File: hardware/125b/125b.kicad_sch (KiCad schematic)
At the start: 49 parts, among them J1 Guitar in, J2 Barrel_Jack, J3 Conn_02x05_Odd_Even_MountingP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, J4 Guitar out, SW1 SW_DIP_x02, SW2 RotaryEncoder_Switch, SW3 Switch 1, SW4 Switch 2, U1 L78L05_TO92, U2 TL074

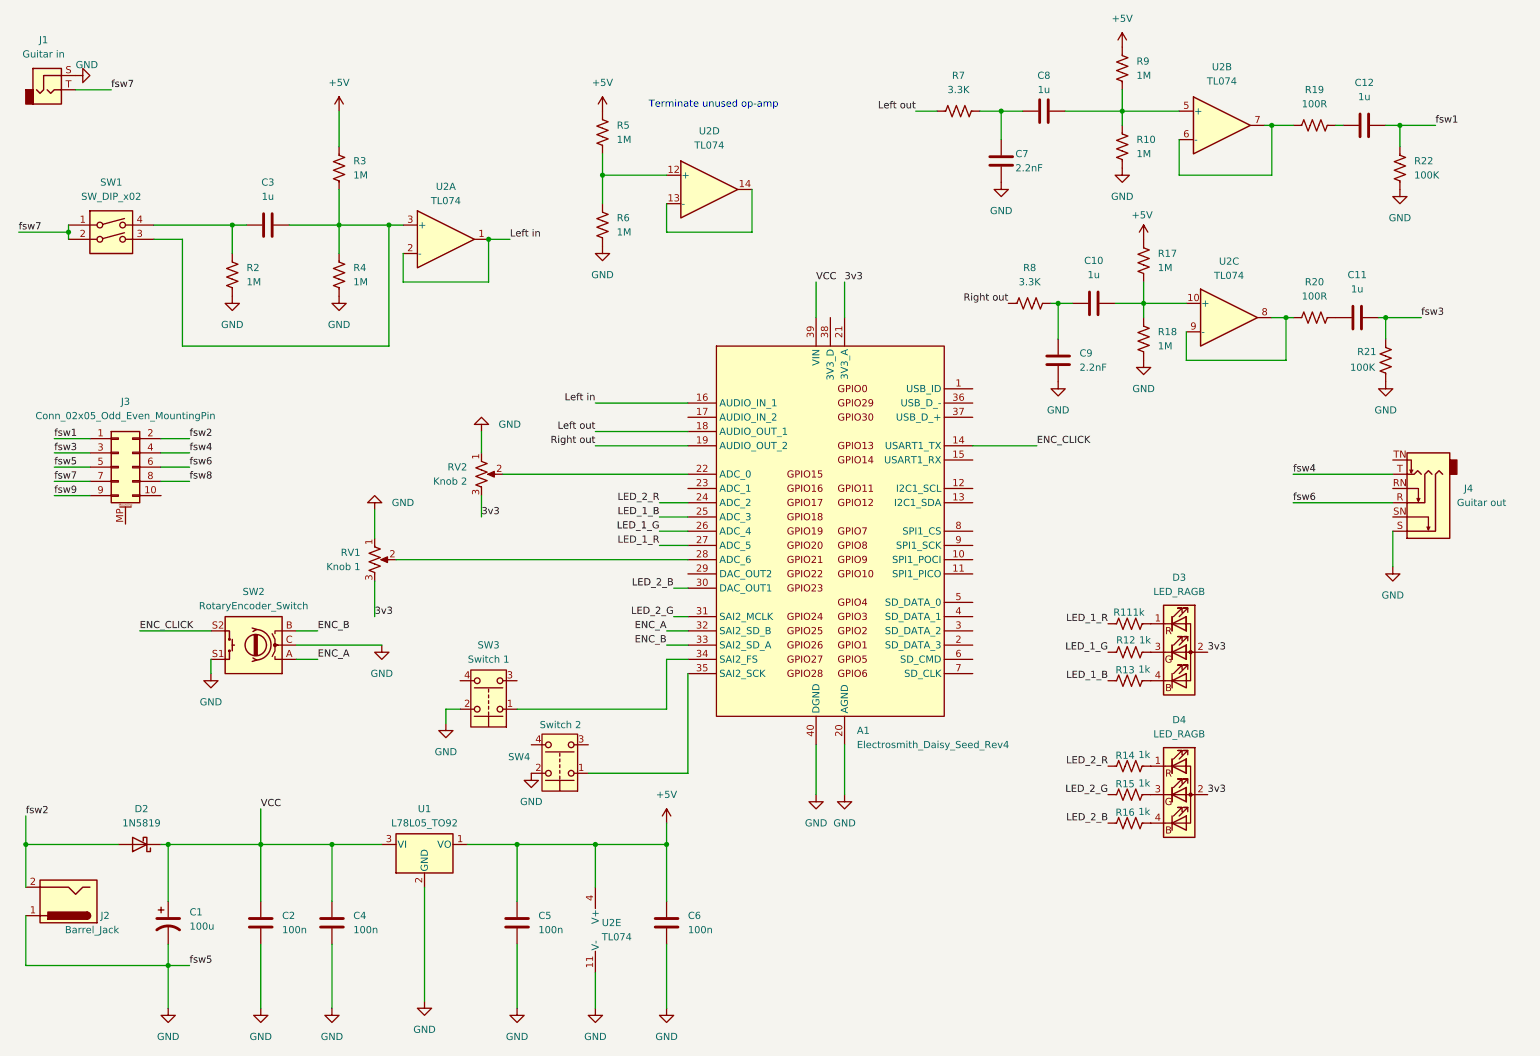
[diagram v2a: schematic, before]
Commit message: All components connected with new IDC socket pos
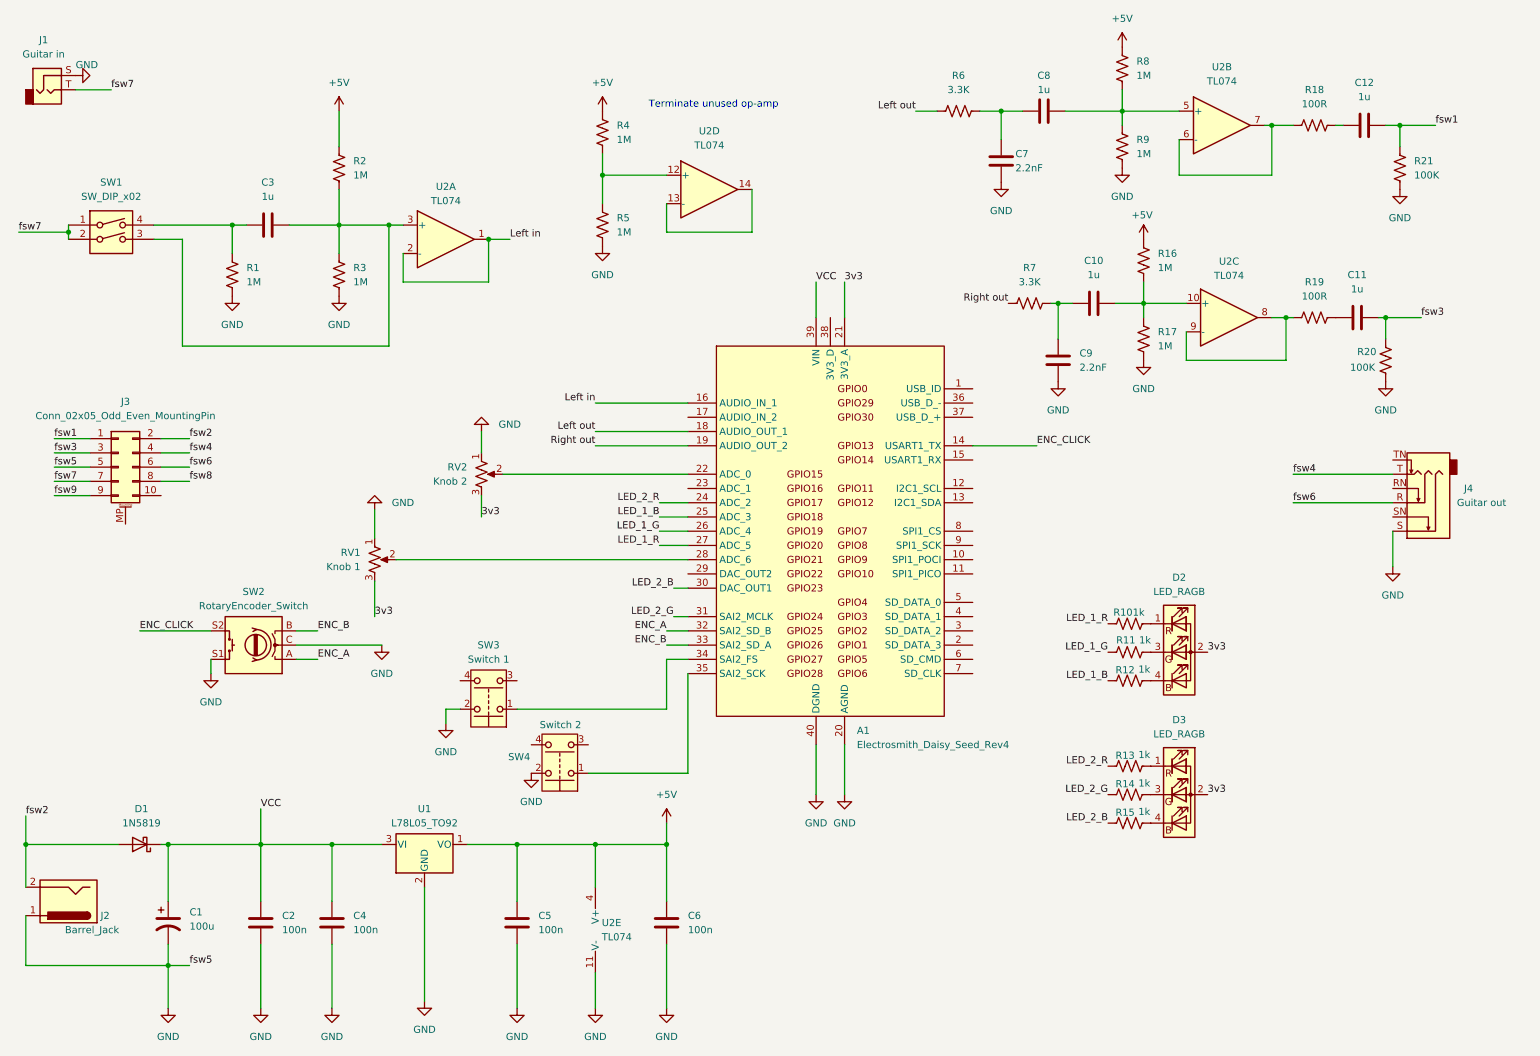
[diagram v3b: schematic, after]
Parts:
- J3: footprint Connector_PinSocket_1.27mm:PinSocket_1x09_P1.27mm_Vertical -> Connector_IDC:IDC-Header_2x05_P2.54mm_Vertical
- renumbered D2 to D1, D3 to D2, D4 to D3, R2 to R1, R11 to R10, R12 to R11, R13 to R12, R14 to R13, R15 to R14, R16 to R15, R17 to R16, R18 to R17, R19 to R18, R20 to R19, R3 to R2, R21 to R20, R22 to R21, R4 to R3, R5 to R4, R6 to R5, R7 to R6, R8 to R7, R9 to R8, R10 to R9
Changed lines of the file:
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@@
 		(on_board yes)
 		(dnp no)
-		(property "Reference" "R12"
+		(property "Reference" "R11"
 			(at 215.265 124.841 90)
 			(effects
@@
 			(project "podal_1590b"
 				(path "/12e895f7-e5ae-4934-aed6-e6e04c63dd03"
-					(reference "R12")
+					(reference "R11")
 					(unit 1)
 				)
@@
 		(on_board yes)
 		(dnp no)
-		(property "Reference" "R14"
+		(property "Reference" "R13"
 			(at 215.138 145.415 90)
 			(effects
@@
 			(project "podal_1590b"
 				(path "/12e895f7-e5ae-4934-aed6-e6e04c63dd03"
-					(reference "R14")
+					(reference "R13")
 					(unit 1)
 				)
@@
 		(dnp no)
 		(fields_autoplaced yes)
-		(property "Reference" "D3"
+		(property "Reference" "D2"
 			(at 224.79 113.665 0)
 			(effects
@@
 			(project "podal_1590b"
 				(path "/12e895f7-e5ae-4934-aed6-e6e04c63dd03"
-					(reference "D3")
+					(reference "D2")
 					(unit 1)
 				)
@@
 		(dnp no)
 		(fields_autoplaced yes)
-		(property "Reference" "R19"
+		(property "Reference" "R18"
 			(at 248.92 26.67 90)
 			(effects
@@
 			(project "podal_1590b"
 				(path "/12e895f7-e5ae-4934-aed6-e6e04c63dd03"
-					(reference "R19")
+					(reference "R18")
 					(unit 1)
 				)
@@
 		(dnp no)
 		(fields_autoplaced yes)
-		(property "Reference" "R3"
+		(property "Reference" "R2"
 			(at 77.47 39.37 0)
 			(effects
@@
 			(project "podal_1590b"
 				(path "/12e895f7-e5ae-4934-aed6-e6e04c63dd03"
-					(reference "R3")
+					(reference "R2")
 					(unit 1)
 				)
@@
 		(on_board yes)
 		(dnp no)
-		(property "Reference" "R13"
+		(property "Reference" "R12"
 			(at 215.138 130.175 90)
 			(effects
@@
 			(project "podal_1590b"
 				(path "/12e895f7-e5ae-4934-aed6-e6e04c63dd03"
-					(reference "R13")
+					(reference "R12")
 					(unit 1)
 				)
@@
 		(dnp no)
 		(fields_autoplaced yes)
-		(property "Reference" "R17"
+		(property "Reference" "R16"
 			(at 220.98 55.88 0)
 			(effects
@@
 			(project "podal_1590b"
 				(path "/12e895f7-e5ae-4934-aed6-e6e04c63dd03"
-					(reference "R17")
+					(reference "R16")
 					(unit 1)
 				)
@@
 		(dnp no)
 		(fields_autoplaced yes)
-		(property "Reference" "R4"
+		(property "Reference" "R3"
 			(at 77.47 58.42 0)
 			(effects
@@
 			(project "podal_1590b"
 				(path "/12e895f7-e5ae-4934-aed6-e6e04c63dd03"
-					(reference "R4")
+					(reference "R3")
 					(unit 1)
 				)
@@
 		(dnp no)
 		(fields_autoplaced yes)
-		(property "Reference" "D4"
+		(property "Reference" "D3"
 			(at 224.79 139.065 0)
 			(effects
@@
 			(project "podal_1590b"
 				(path "/12e895f7-e5ae-4934-aed6-e6e04c63dd03"
-					(reference "D4")
+					(reference "D3")
 					(unit 1)
 				)
@@
 		(dnp no)
 		(fields_autoplaced yes)
-		(property "Reference" "R18"
+		(property "Reference" "R17"
 			(at 220.98 69.85 0)
 			(effects
@@
 			(project "podal_1590b"
 				(path "/12e895f7-e5ae-4934-aed6-e6e04c63dd03"
-					(reference "R18")
+					(reference "R17")
 					(unit 1)
 				)
@@
 		(on_board yes)
 		(dnp no)
-		(property "Reference" "R8"
+		(property "Reference" "R7"
 			(at 198.12 58.42 90)
 			(effects
@@
 			(project "podal_1590b"
 				(path "/12e895f7-e5ae-4934-aed6-e6e04c63dd03"
-					(reference "R8")
+					(reference "R7")
 					(unit 1)
 				)
@@
 		(on_board yes)
 		(dnp no)
-		(property "Reference" "R21"
+		(property "Reference" "R20"
 			(at 256.54 73.406 0)
 			(effects
@@
 			(project "podal_1590b"
 				(path "/12e895f7-e5ae-4934-aed6-e6e04c63dd03"
-					(reference "R21")
+					(reference "R20")
 					(unit 1)
 				)
@@
 		(dnp no)
 		(fields_autoplaced yes)
-		(property "Reference" "R9"
+		(property "Reference" "R8"
 			(at 217.17 21.59 0)
 			(effects
@@
 			(project "podal_1590b"
 				(path "/12e895f7-e5ae-4934-aed6-e6e04c63dd03"
-					(reference "R9")
+					(reference "R8")
 					(unit 1)
 				)
@@
 		(dnp no)
 		(fields_autoplaced yes)
-		(property "Reference" "R2"
+		(property "Reference" "R1"
 			(at 58.42 58.42 0)
 			(effects
@@
 			(project "podal_1590b"
 				(path "/12e895f7-e5ae-4934-aed6-e6e04c63dd03"
-					(reference "R2")
+					(reference "R1")
 					(unit 1)
 				)
@@
 			)
 		)
-		(property "Footprint" "Connector_PinSocket_1.27mm:PinSocket_1x09_P1.27mm_Vertical"
+		(property "Footprint" "Connector_IDC:IDC-Header_2x05_P2.54mm_Vertical"
 			(at 35.56 93.98 0)
 			(effects
@@
 		(dnp no)
 		(fields_autoplaced yes)
-		(property "Reference" "R6"
+		(property "Reference" "R5"
 			(at 124.46 49.53 0)
 			(effects
@@
 			(project "podal_1590b"
 				(path "/12e895f7-e5ae-4934-aed6-e6e04c63dd03"
-					(reference "R6")
+					(reference "R5")
 					(unit 1)
 				)
@@
 		(dnp no)
 		(fields_autoplaced yes)
-		(property "Reference" "R22"
+		(property "Reference" "R21"
 			(at 266.7 39.37 0)
 			(effects
@@
 			(project "podal_1590b"
 				(path "/12e895f7-e5ae-4934-aed6-e6e04c63dd03"
-					(reference "R22")
+					(reference "R21")
 					(unit 1)
 				)
@@
 		(on_board yes)
 		(dnp no)
-		(property "Reference" "R15"
+		(property "Reference" "R14"
 			(at 215.138 150.495 90)
 			(effects
@@
 			(project "podal_1590b"
 				(path "/12e895f7-e5ae-4934-aed6-e6e04c63dd03"
-					(reference "R15")
+					(reference "R14")
 					(unit 1)
 				)
@@
 		(on_board yes)
 		(dnp no)
-		(property "Reference" "R16"
+		(property "Reference" "R15"
 			(at 215.138 155.575 90)
 			(effects
@@
 			(project "podal_1590b"
 				(path "/12e895f7-e5ae-4934-aed6-e6e04c63dd03"
-					(reference "R16")
+					(reference "R15")
 					(unit 1)
 				)
@@
 		(dnp no)
 		(fields_autoplaced yes)
-		(property "Reference" "R20"
+		(property "Reference" "R19"
 			(at 248.92 60.96 90)
 			(effects
@@
 			(project "podal_1590b"
 				(path "/12e895f7-e5ae-4934-aed6-e6e04c63dd03"
-					(reference "R20")
+					(reference "R19")
 					(unit 1)
 				)
@@
 		(on_board yes)
 		(dnp no)
-		(property "Reference" "R11"
+		(property "Reference" "R10"
 			(at 214.757 119.888 90)
 			(effects
@@
 			(project "podal_1590b"
 				(path "/12e895f7-e5ae-4934-aed6-e6e04c63dd03"
-					(reference "R11")
+					(reference "R10")
 					(unit 1)
 				)
@@
 		(dnp no)
 		(fields_autoplaced yes)
-		(property "Reference" "R10"
+		(property "Reference" "R9"
 			(at 217.17 35.56 0)
 			(effects
@@
 			(project "podal_1590b"
 				(path "/12e895f7-e5ae-4934-aed6-e6e04c63dd03"
-					(reference "R10")
+					(reference "R9")
 					(unit 1)
 				)
@@
 		(on_board yes)
 		(dnp no)
-		(property "Reference" "R7"
+		(property "Reference" "R6"
 			(at 185.42 24.13 90)
 			(effects
@@
 			(project "podal_1590b"
 				(path "/12e895f7-e5ae-4934-aed6-e6e04c63dd03"
-					(reference "R7")
+					(reference "R6")
 					(unit 1)
 				)
@@
 		(dnp no)
 		(fields_autoplaced yes)
-		(property "Reference" "D2"
+		(property "Reference" "D1"
 			(at 39.6875 154.94 0)
 			(effects
@@
 			(project "podal_1590b"
 				(path "/12e895f7-e5ae-4934-aed6-e6e04c63dd03"
-					(reference "D2")
+					(reference "D1")
 					(unit 1)
 				)
@@
 		(dnp no)
 		(fields_autoplaced yes)
-		(property "Reference" "R5"
+		(property "Reference" "R4"
 			(at 124.46 33.02 0)
 			(effects
@@
 			(project "podal_1590b"
 				(path "/12e895f7-e5ae-4934-aed6-e6e04c63dd03"
-					(reference "R5")
+					(reference "R4")
 					(unit 1)
 				)
